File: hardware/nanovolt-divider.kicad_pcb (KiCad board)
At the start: 2 copper layers, 60 x 103 mm, 76 parts, among them J1 NORMAL IN +, J2 NORMAL IN -, J3 HV IN +, J4 HV IN -, J5 DIVIDER OUT HI, J6 DIVIDER OUT LO, J7 ESP32_DISP_P1, J8 ESP32_DISP_CN1, J9 ESP32_DISP_P3, K1 TQ2-L2-5V, K2 TQ2-L2-5V, K3 TQ2-L2-5V, K4 TQ2-L2-5V, K5 TQ2-L2-5V, Q1 MMBT2222A, Q10 MMBT2222A, Q2 MMBT2222A, Q3 MMBT2222A, Q4 MMBT2222A, Q5 MMBT2222A, Q6 MMBT2222A, Q7 MMBT2222A, Q8 MMBT2222A, Q9 MMBT2222A, SW1 SW_3PDT NORMAL/HV, U1 MCP23017-E/SO, U2 TMP117MAIYBGR

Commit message: Rev0: named analog nets, both relay poles, HV netclass, smaller board
Restore the HV netclass (the real bug)
--------------------------------------
nanovolt-divider.kicad_dru conditions all three 450 V rules on NetClass == 'HV',
but the project file had "netclass_patterns": [] and no HV class, so every one of
them matched nothing. DRC reported "0 violations" whether the board was safe or
not. The original patterns matched auto-generated names like Net-(J3-Pin_1) and
were dropped when KiCad rewrote the project file.

The class is back with the patterns spelled out - /HV_IN_P and /HV_DIV, never a
"HV*" wildcard, which would sweep in HV_SENSE (a 3.3 V logic line). Verified by
moving R34 next to K5 on a scratch copy and confirming the rules fire; restoring
them immediately exposed 25 real clearance/creepage violations in the old
placement, now fixed.

gen_schematics.py no longer overwrites .kicad_pro (write_once): it emits a
25-line stub, and KiCad owns the 702-line file that holds the netclass.

Schematic
---------
* Analog nets carry real labels instead of /POLARITY (K4)/A_COM and
  Net-(J4-Pin_1): SRC_P, SRC_RTN, NORMAL_IN_P/N, RANGE_BUS, R*_IN, R*_OUT,
  INJ_NODE, MEAS_NODE, ANALOG_RTN, HV_IN_P, HV_DIV. This is also what gives the
  HV netclass stable patterns to match.
* K1..K3 use both poles: SRC_P -> A_COM -> A_NO -> R -> B_NO -> B_COM ->
  RANGE_BUS, so a deselected high leg is isolated at both ends.
* Control ground is DGND, not the global GND, so it cannot merge with the
  floating analog return.
* J7/J8/J9 use project symbols with the module's own pin names (SCL_IO22, IO35)
  instead of Conn_01x04 Pin_1..Pin_4. Pin geometry is unchanged, so no wire moved.
* Removed from the board: J4 (HV IN- is a panel-to-panel wire to SW1 lug 6), R26
  and SW1 lug 7 (R25's 100k already holds HV_SENSE low off the HV throw). Added
  C5 10 nF to stiffen the 100k against pickup on the IO35 harness. The two
  off-board lugs are documented in a panel-wiring note on the root sheet.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
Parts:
- removed J4: HV IN -, Connector_Wire:SolderWire-0.25sqmm_1x01_D0.65mm_OD1.7mm
- removed R26: 10k, Resistor_SMD:R_1206_3216Metric
- added C5: 10n, Capacitor_SMD:C_1206_3216Metric, F.Cu at (104.5, 63.5)
- SW1: footprint nanovolt-divider:SW_3PDT_WirePads_3x3_P7.62mm -> nanovolt-divider:SW_3PDT_WirePads_Split
- moved R34 19.4 mm to (106.0, 114.0), turned to -90 degrees
- moved H3 19.0 mm to (53.0, 131.0)
- moved H4 19.0 mm to (107.0, 131.0)
- moved SW1 18.0 mm to (73.5, 124.0)
- moved J3 7.50 mm to (98.0, 114.0)
- moved R31 6.38 mm to (69.8, 111.0), turned to -90 degrees
- moved J2 3.20 mm to (53.0, 118.0)
- moved R32 3.16 mm to (80.0, 111.0), turned to -90 degrees
- moved J1 2.50 mm to (53.0, 112.0)
- moved C2 2.00 mm to (84.5, 139.5)
- moved J5 2.00 mm to (95.5, 145.0)
- moved J6 2.00 mm to (64.5, 145.0)
- moved R35 2.00 mm to (69.8, 145.0)
- moved U2 2.00 mm to (80.0, 139.5)
- moved R33 1.64 mm to (90.2, 111.0), turned to -90 degrees
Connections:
- net /INJECT (K5)/A_NO renamed /INJ_NODE
- net /POLARITY (K4)/A_COM renamed /SRC_P
- net /POLARITY (K4)/A_NC renamed /NORMAL_IN_P
- net /POLARITY (K4)/A_NO renamed /NORMAL_IN_N
- net /POLARITY (K4)/B_COM renamed /SRC_RTN
- net /RANGE_1E5 (K1)/A_NO renamed /R100K_IN
- net /RANGE_1E6 (K2)/A_NO renamed /R1M_IN
- net /RANGE_1E7 (K3)/A_NO renamed /R10M_IN
- net GND renamed DGND
- net Net-(J3-Pin_1) renamed /HV_IN_P
- net Net-(J5-Pin_1) renamed /MEAS_NODE
- net Net-(J6-Pin_1) renamed /ANALOG_RTN
- net Net-(SW1A-HV) renamed /HV_DIV
- K1 pad 7: /RANGE_1E5 (K1)/B_NO -> /R100K_OUT
- K1 pad 8: /RANGE_1E5 (K1)/B_COM -> /RANGE_BUS
- K2 pad 7: /RANGE_1E6 (K2)/B_NO -> /R1M_OUT
- K2 pad 8: /RANGE_1E6 (K2)/B_COM -> /RANGE_BUS
- K3 pad 7: /RANGE_1E7 (K3)/B_NO -> /R10M_OUT
- K3 pad 8: /RANGE_1E7 (K3)/B_COM -> /RANGE_BUS
- K5 pad 3: /INJECT (K5)/A_COM -> /RANGE_BUS
- R31 pad 2: /INJECT (K5)/A_COM -> /R100K_OUT
- R32 pad 2: /INJECT (K5)/A_COM -> /R1M_OUT
- R33 pad 2: /INJECT (K5)/A_COM -> /R10M_OUT
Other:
- board size 60 x 103 mm -> 60 x 100 mm
- board text added: "RANGE CELLS"
- board text added: "SW 3PDT"
- board text removed: "PRECISION / QUIET"

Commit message: K5 pole B breaks the return leg: ISOLATE now opens both sides
Pole A already broke the high side (RANGE_BUS -> INJ_NODE); pole B was unused
with all three pins no-connect. It now breaks the return in step with it:
SRC_RTN -> K5 B_COM, K5 B_NO -> INJ_RTN -> 3PDT pole 2 NORMAL throw.

In ISOLATE the programmable source is now detached from the 1 ohm and the DMM
path at both ends, so none of it - output capacitance, cabling, leakage to earth
- stays attached to the measurement node.

SRC_RTN and INJ_RTN are carried by net label rather than a polyline: a drawn wire
from K5 pole B across to the switch would have to cross both INJ_NODE and HV_DIV.

Net changes: /SRC_RTN is now K4.8 + K5.8 (was K4.8 + SW1.4); /INJ_RTN is new
(K5.7 + SW1.4). K5 A_NC and B_NC remain no-connect. Nothing else moved.

ERC 0, DRC 0 errors, 0 schematic-parity issues; HV netclass intact.

Co-Authored-By: Claude Opus 5 <noreply@anthropic.com>
Claude-Session: https://claude.ai/code/session_0168vwTBRM7XaQRxDqmVSFLB
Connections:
- K5 pad 7: /INJECT (K5)/B_NO -> /INJ_RTN
- K5 pad 8: /INJECT (K5)/B_COM -> /SRC_RTN
- SW1 pad 4: /SRC_RTN -> /INJ_RTN
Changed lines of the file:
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@@
 			(layers "*.Cu" "*.Mask")
 			(remove_unused_layers no)
-			(net "/SRC_RTN")
+			(net "/INJ_RTN")
 		)
 		(pad "5" thru_hole circle
@@
 			(layers "*.Cu" "*.Mask")
 			(remove_unused_layers no)
-			(net "/INJECT (K5)/B_NO")
+			(net "/INJ_RTN")
 		)
 		(pad "8" thru_hole circle
@@
 			(layers "*.Cu" "*.Mask")
 			(remove_unused_layers no)
-			(net "/INJECT (K5)/B_COM")
+			(net "/SRC_RTN")
 		)
 		(pad "9" thru_hole circle

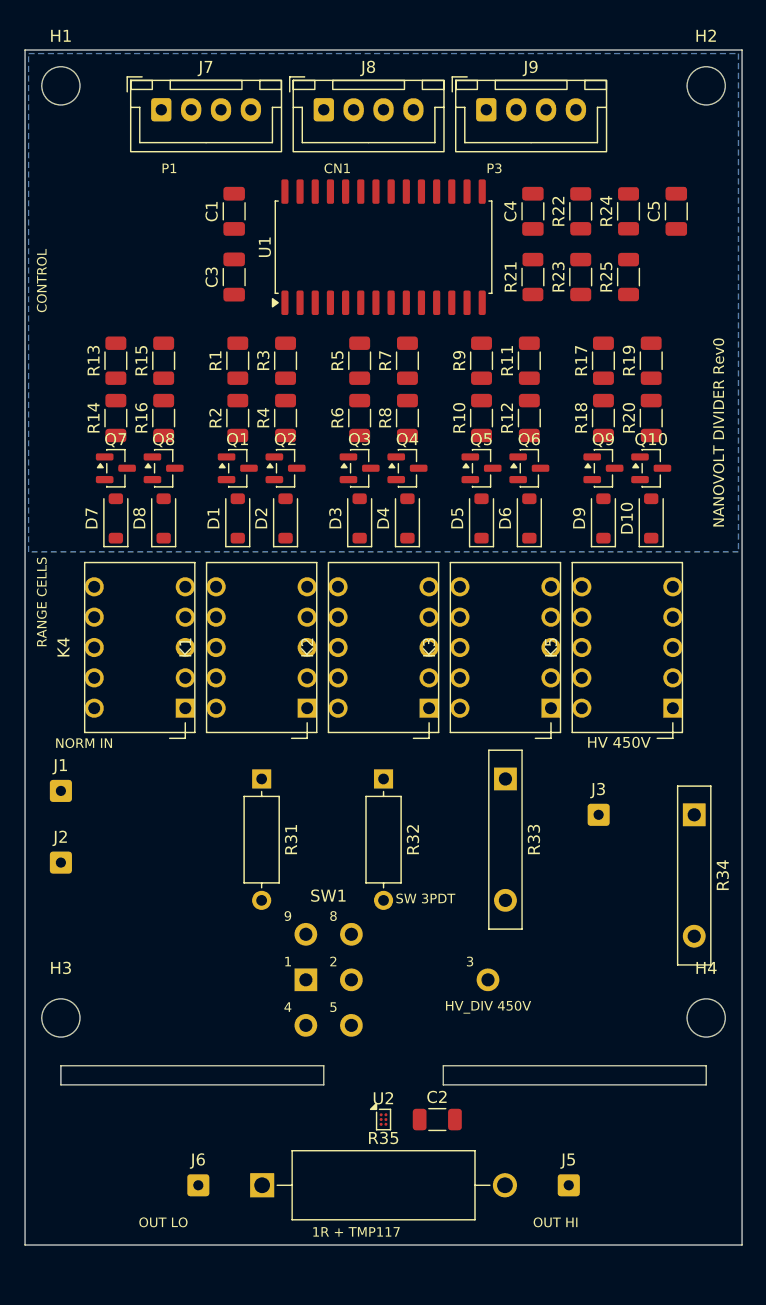
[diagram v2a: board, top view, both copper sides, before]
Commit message: Solder the display harness: J7-J9 become wire pads, board shrinks to 60x94
The board specified JST_XH_B4B-XH-A (2.50 mm) for J7/J8/J9, but the
ESP32-2432S028R's P1/CN1/P3 are 1.25 mm-class connectors.  That header
never mated with anything: it meant crimping a bespoke pitch-bridging
cable for a joint that never needs to unmate.  Solder the module's own
supplied pigtail to the board instead and the header, the crimping and
the pitch mismatch all go away at once.  The module end keeps its
connector, so the display still unplugs.

This also makes the board consistent - J1/J2/J3/J5/J6 are already
SolderWire pads and SW1 is a wire-pad footprint.  J7-J9 were the only
mateable connectors left on it.

Only the 8 live conductors get pads (J7 = P1 pins 3/4, J8 = CN1 pins
1-4, J9 = P3 pins 1/2), and each pad keeps the module's own pin number
rather than being renumbered 1..n, so the schematic still reads "this
wire lands on module P1 pin 3".  All three GND wires stay: P1's returns
the pulsed coil current, P3's is the HV_SENSE reference, CN1's serves
I2C - one net, but three conductors cut the cable-side IR drop.

Flat pads delete the top row's 5.75 mm bodies and their mating envelope,
freeing 6 mm: 60x100 -> 60x94, applied as one SHIFT_Y translation so
every reviewed relative spacing (slot geometry, HV island separation,
the 1 ohm strip, bridge widths) is unchanged.

Two things the regeneration turned up:
  * C5 landed 0.3 mm inside the top-right M3 hole's courtyard after the
    shift.  Moved to the second sub-row beside R25, its own pulldown.
  * The harness refdes silk ran off the board edge.  With the row 2.5 mm
    from the top there is one usable silk line below the pads, so it
    carries the module connector name (P1/CN1/P3) - what someone landing
    bare conductors actually needs - and the refdes moved to F.Fab.

Verified: ERC 0 violations.  DRC identical to the pre-change baseline
(67 pre-existing silk-over-copper on the unrouted board, 150 unconnected).
Netlist dif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
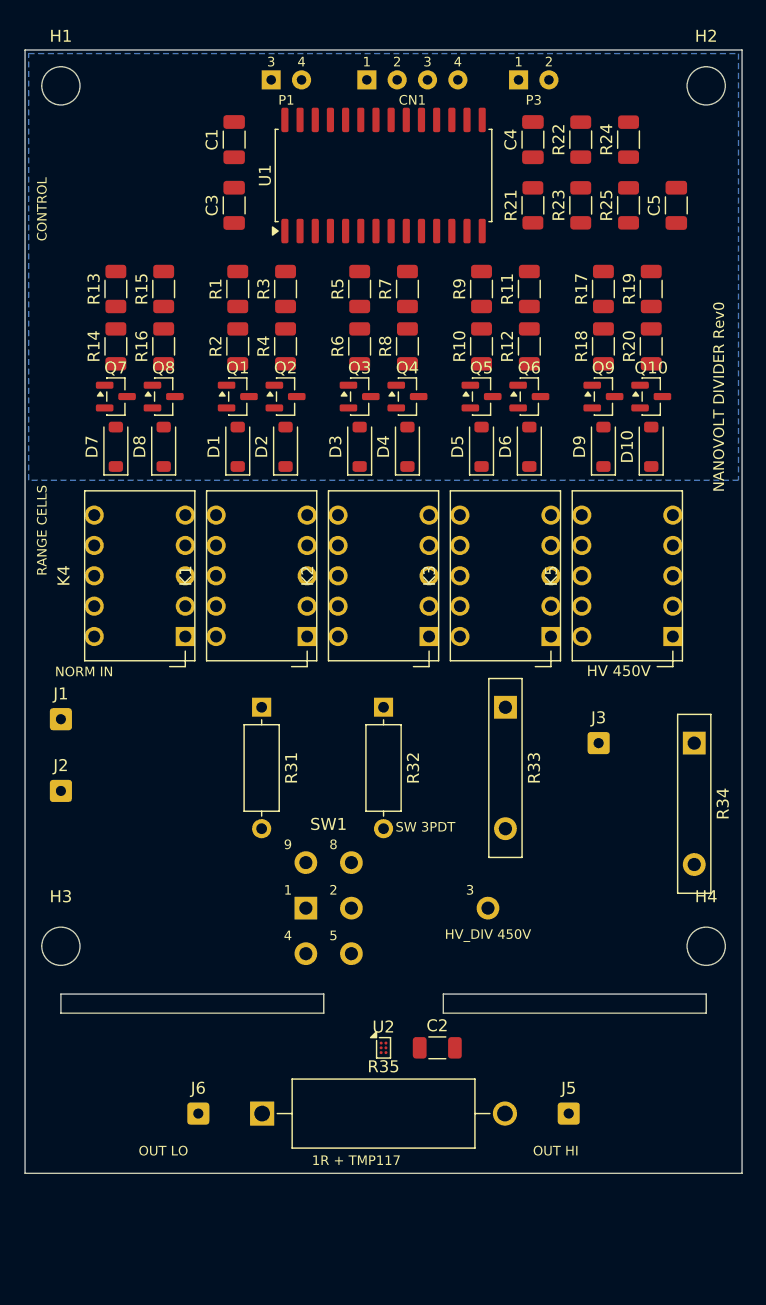
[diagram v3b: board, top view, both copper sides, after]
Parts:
- J7: footprint Connector_JST:JST_XH_B4B-XH-A_1x04_P2.50mm_Vertical -> nanovolt-divider:J_ESP32_P1_WirePads
- J8: footprint Connector_JST:JST_XH_B4B-XH-A_1x04_P2.50mm_Vertical -> nanovolt-divider:J_ESP32_CN1_WirePads
- J9: footprint Connector_JST:JST_XH_B4B-XH-A_1x04_P2.50mm_Vertical -> nanovolt-divider:J_ESP32_P3_WirePads
- moved J7 9.53 mm to (70.6, 52.5)
- moved C1 6.00 mm to (67.5, 57.5)
- moved C2 6.00 mm to (84.5, 133.5)
- moved C3 6.00 mm to (67.5, 63.0)
- moved C4 6.00 mm to (92.5, 57.5)
- moved D1 6.00 mm to (67.8, 83.2)
- moved D10 6.00 mm to (102.4, 83.2)
- moved D2 6.00 mm to (71.8, 83.2)
- moved D3 6.00 mm to (78.0, 83.2)
- moved D4 6.00 mm to (82.0, 83.2)
- moved D5 6.00 mm to (88.2, 83.2)
- moved D6 6.00 mm to (92.2, 83.2)
- moved D7 6.00 mm to (57.6, 83.2)
- moved D8 6.00 mm to (61.6, 83.2)
- moved D9 6.00 mm to (98.4, 83.2)
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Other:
- board size 60 x 100 mm -> 60 x 94 mm
- board text removed: "CN1"
- board text removed: "P1"
- board text removed: "P3"

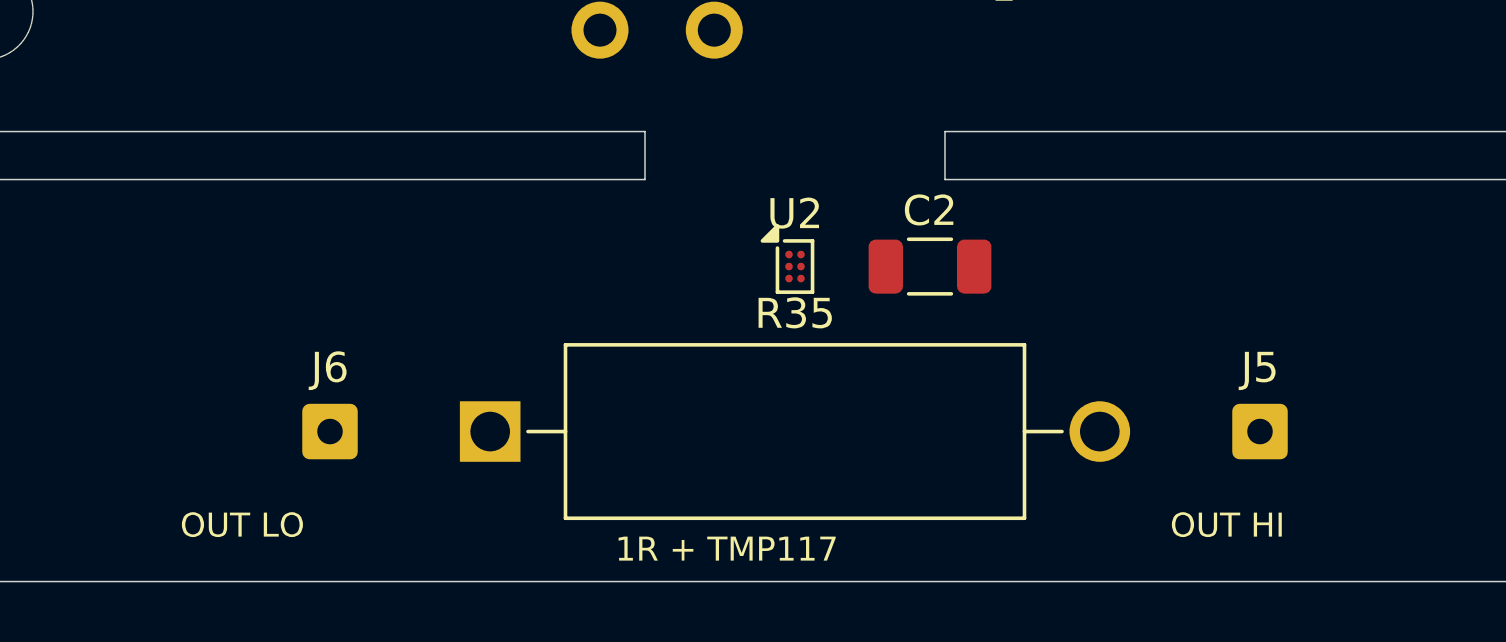
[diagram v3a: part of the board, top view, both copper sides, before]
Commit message: Swap the TMP117 for a TMP275: SOIC-8, so it can be hand-soldered
The TMP117 only ships as a DSBGA-6 on a 0.4 mm ball pitch, which is not
hand-assemblable, and this board is built by hand. TMP275AIDR is SOIC-8
at 1.27 mm pitch and keeps address 0x48 (A2:A0 all on DGND), so nothing
else on the I2C bus moves.

The cost is absolute accuracy: +/-0.5 C and 12-bit (0.0625 C) instead of
+/-0.1 C and 16-bit (0.0078 C). That is not what this sensor is for - it
tracks the *change* in the 1 ohm region's temperature for the optional
ratio correction, and that needs short-term repeatability, not absolute
accuracy. The register map is not TMP117-compatible, so firmware will
differ when it is written.

Schematic: new project symbol nanovolt-divider:TMP275. KiCad 10 has no
TMP275 - the pinout is the LM75/TMP75 industry-standard one, so
Sensor_Temperature:LM75B would have wired up correctly, but it would put
"LM75B" in the lib_id and call pin 3 "O.S." instead of ALERT. The body is
17.78 mm wide so the rotated V+ / GND pin names clear "ALERT".

Board: a SOIC-8 courtyard is 5.4 mm tall and the band between the
isolation slots and R35 was 5.38 mm, so the sensor no longer fits in the
gap over the resistor body. It sits on the same thermally isolated island
above R35, centred on the resistor's midpoint, 0.7 mm below the slots and
0.8 mm above R35's courtyard - the island is what couples it to R35, not
the millimetre of air over the body. The 1 ohm row dropped 1.5 mm to make
the room, taken from the bottom margin so the slots, the mounting holes
and everything above them stay where the Rev0 review left them.

U2's designator moves to F.Fab and R35's to its pad-1 end (new
REF_OVERRIDE table in gen_pcb.py): there is no silk line left between a
SOIC-8 and a 20 mm resistor sharing a 6.9 mm band. The DSBGA 0.1 mm
intra-footprint DRC exception is gone from the .kicad_dru with the part
that needed it.

ERC 0 violations. The netlist diff is confined to U2's pins. DRC 66
violations against a 67 bas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
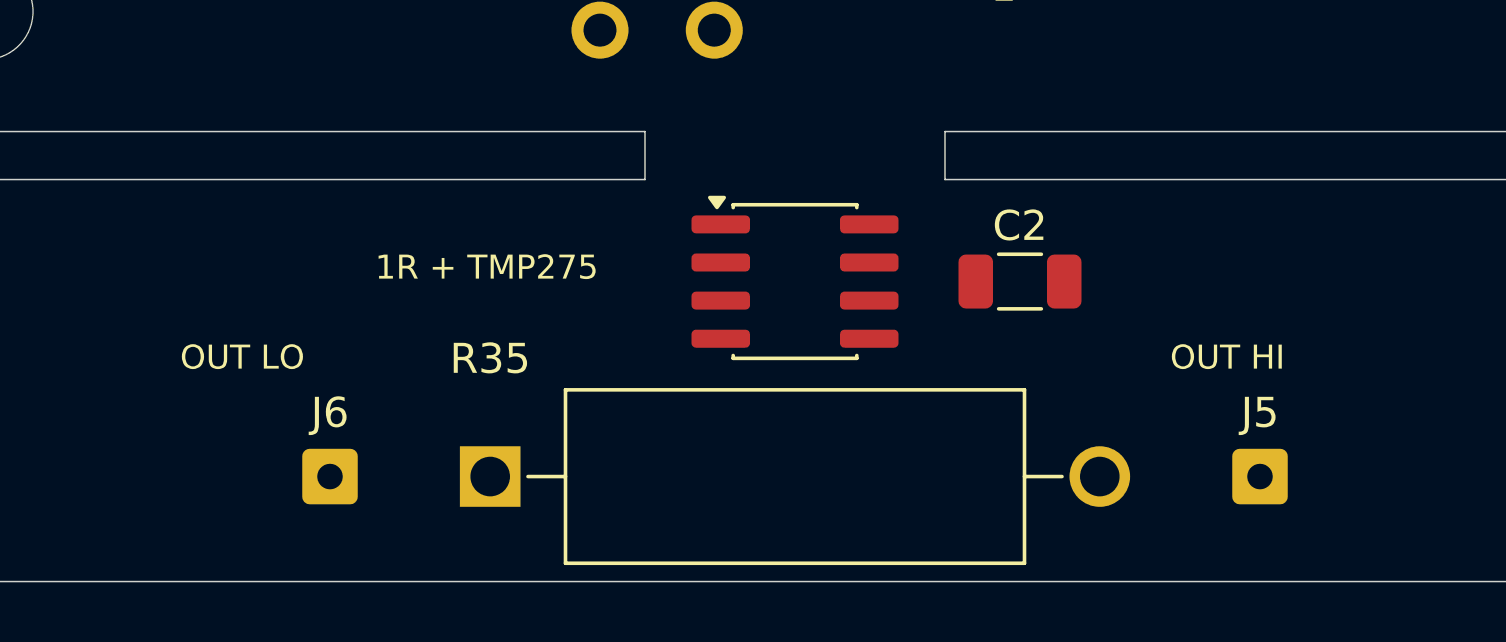
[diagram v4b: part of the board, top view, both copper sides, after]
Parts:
- U2: value TMP117MAIYBGR -> TMP275AIDR; footprint Package_BGA:Texas_DSBGA-6_0.95x1.488mm_Layout2x3_P0.4mm -> Package_SO:SOIC-8_3.9x4.9mm_P1.27mm
- moved C2 3.04 mm to (87.5, 134.0)
- moved J5 1.50 mm to (95.5, 140.5)
- moved J6 1.50 mm to (64.5, 140.5)
- moved R35 1.50 mm to (69.8, 140.5)
- moved U2 0.50 mm to (80.0, 134.0)
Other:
- board text added: "1R + TMP275"
- board text removed: "1R + TMP117"
